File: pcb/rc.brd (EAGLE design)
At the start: 40.6 x 58.4 mm, 57 parts, among them IC2 TP4056

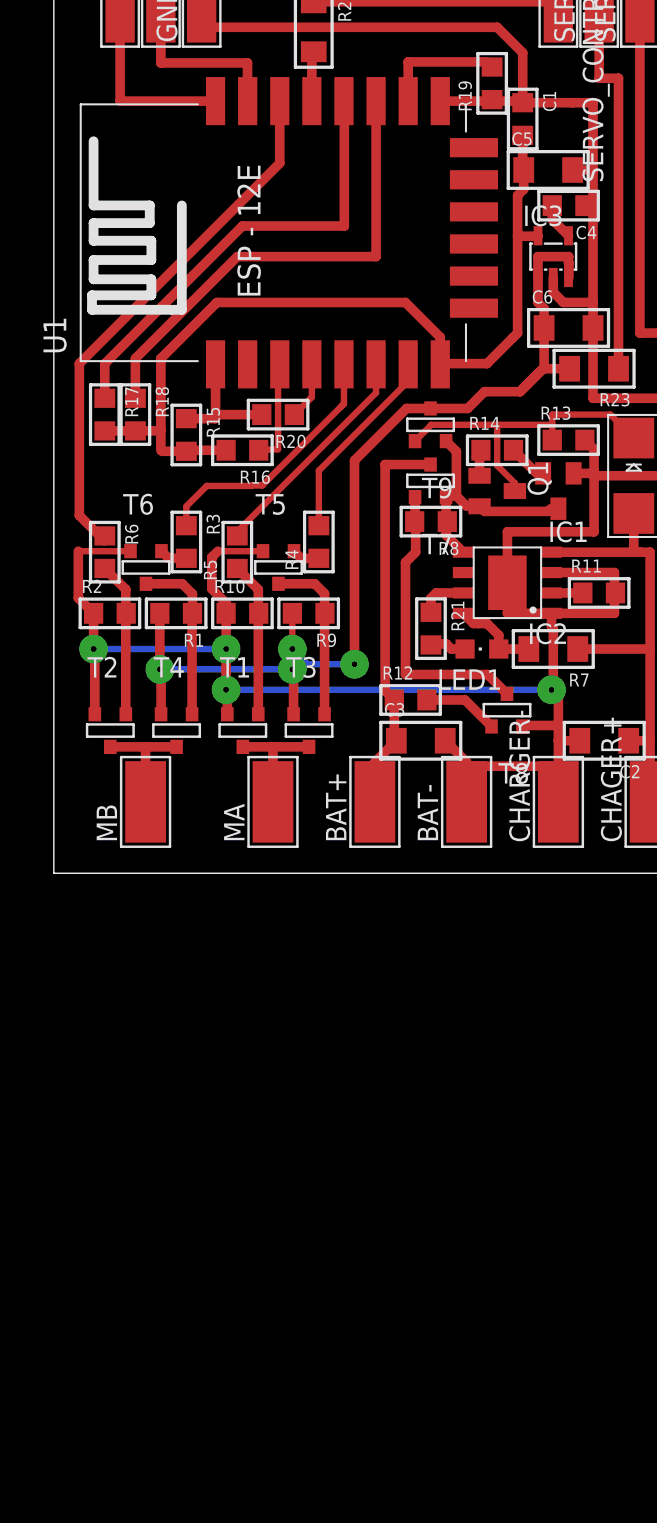
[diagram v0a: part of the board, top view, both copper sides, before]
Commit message: scheme: change H-bridge and battety check
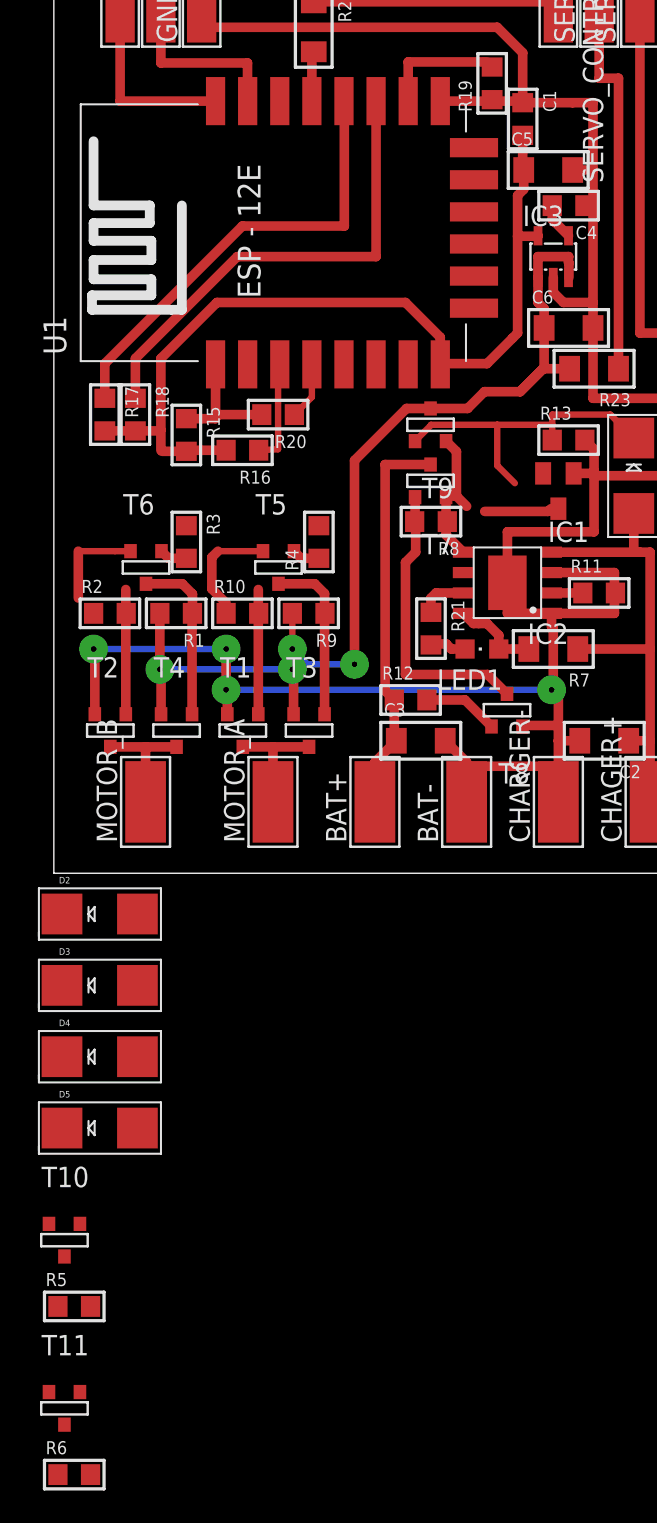
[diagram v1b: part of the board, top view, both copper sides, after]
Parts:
- removed Q1: (no value), semicon-smd-ipc:SOT23
- removed R14: (no value), skydrop:R0805
- added D2, D3, D4, D5: (no value), skydrop:SMADIODE
- added T10, T11: (no value), zetex:SOT-23
- moved R6 57.5 mm to (1.27, -33.0), turned to 0 degrees
- moved R5 48.1 mm to (1.27, -22.5), turned to 0 degrees
- renumbered MA to MOTOR_A, MB to MOTOR_B
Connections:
- removed net H_LN: R5.2, U1.GPIO12
- removed net H_LP: R4.2, U1.GPIO13
- removed net H_RN: R6.1, U1.GPIO5
- removed net H_RP: R3.1, U1.GPIO14
- new net BAT_CHECK: T11.1, U1.GPIO12
- new net H_BCK: R3.1, U1.GPIO13
- new net H_FWD: R4.2, U1.GPIO14
- new net H_PWM: R5.2, U1.GPIO5
- new net N$31: D4.C, D5.C, T10.1
- new net N$32: R5.1, T10.3
- net BAT_PROT: now also R10.1, R2.1
- net GND: now also T10.2, T11.2; no longer R10.1, R2.1
- net N$1: now also D2.C
- net N$10: no longer Q1.2
- net N$13: now also R6.2, T11.3; no longer Q1.1, R14.1
- net N$17: now also R6.1; no longer R14.2
- net N$24: no longer Q1.3
- net N$6: now also D2.A, D4.A; no longer R5.1
- net N$8: now also D3.C
- net N$9: now also D3.A, D5.A; no longer R6.2
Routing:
- net H_RN: track 33.6 -> 0.00 mm
- net H_RP: track 16.4 -> 0.00 mm
- net H_LN: track 14.3 -> 0.00 mm
- net H_LP: track 12.4 -> 0.00 mm
- net GND: track 219.5 -> 213.1 mm
- net N$17: track 2.44 -> 0.00 mm
- net N$9: track 9.65 -> 7.80 mm
- net N$6: track 9.70 -> 7.85 mm
- net N$13: track 1.71 -> 0.00 mm
- net N$10: track 15.4 -> 14.1 mm

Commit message: begin pcb v2
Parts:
- removed CHAGER+, CHARGER-: WIREPADSMD5-2,5, wirepad:5-2,5
- removed D1, D5: (no value), skydrop:SMADIODE
- added D6: (no value), skydrop:SOD-123FL
- added J1: (no value), skydrop:USB-AB-MICRO-SMD
- added R14: 0, skydrop:R1206
- added R24: (no value), skydrop:R1206
- D2, D3, D4: device skydrop:SMADIODE -> skydrop:SOD-123FL
- moved GND 54.7 mm to (5.40, 4.13), flipped to the bottom, turned to 180 degrees
- moved RX 54.7 mm to (2.86, 4.13), flipped to the bottom, turned to 0 degrees
- moved TX 54.7 mm to (0.32, 4.13), flipped to the bottom, turned to 0 degrees
- moved SERVO_CONTROL 51.8 mm to (28.9, 6.99), flipped to the bottom, turned to 0 degrees
- moved SERVO_GND 51.8 mm to (34.0, 6.99), flipped to the bottom, turned to 180 degrees
- moved SERVO_POWER 51.8 mm to (31.4, 6.99), flipped to the bottom, turned to 180 degrees
- moved R22 48.6 mm to (15.2, 8.57), flipped to the bottom, turned to 90 degrees
- moved R5 46.4 mm to (7.30, 23.5), turned to 90 degrees
- moved R6 41.9 mm to (18.7, 5.08), turned to 90 degrees
- moved T10 41.7 mm to (3.81, 23.2), turned to 90 degrees
- moved R19 41.7 mm to (24.8, 12.1), flipped to the bottom, turned to 270 degrees
- moved T11 39.2 mm to (21.3, 4.45), turned to 90 degrees
- moved C1 37.2 mm to (26.7, 14.3), flipped to the bottom, turned to 90 degrees
- moved C5 30.9 mm to (28.3, 17.5), flipped to the bottom, turned to 180 degrees
- moved IC1 29.0 mm to (15.9, 3.81), turned to 90 degrees
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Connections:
- net N$14 renamed BAT+
- net N$15 renamed TX
- net N$18 renamed RX
- removed net N$10: IC1.3, IC2.5, R8.1, T7.2, T9.2
- removed net N$24: D1.C, R13.1, T9.3
- new net BAT_CHRG: IC2.5, R8.1, T7.2, T9.2
- new net N$14: R14.1, T11.1
- net BAT_CHECK: now also R14.2; no longer T11.1
- net BAT_PROT: now also IC1.3
- net GND: now also J1.GND; no longer CHARGER-.1
- net N$31: now also D6.C; no longer D5.C
- net N$9: now also D6.A; no longer D5.A
- net V_CHRG: now also J1.VBUS, R13.1, R24.1, R24.2, T9.3; no longer CHAGER+.1, D1.A
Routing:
- net H_BCK: track 0.00 -> 51.2 mm, vias 0 -> 1
- net H_PWM: track 0.00 -> 49.7 mm, vias 0 -> 1
- net BAT_CHECK: track 0.00 -> 29.0 mm, vias 0 -> 1
- net N$24: track 20.4 -> 0.00 mm
- net N$12: track 19.1 -> 4.25 mm
- net GND: track 213.1 -> 198.3 mm, vias 4 -> 5
- net N$10: track 14.1 -> 0.00 mm
- net N$29: track 15.3 -> 1.59 mm
- net H_FWD: track 0.00 -> 13.3 mm, vias 0 -> 1
- net N$31: track 0.00 -> 10.4 mm
- net BAT_PROT: track 66.2 -> 56.8 mm, vias 4 -> 3
- net BAT_CHRG: track 0.00 -> 8.83 mm
- net RX: track 11.6 -> 19.9 mm
- net V_CHRG: track 30.5 -> 23.4 mm
- net TX: track 12.1 -> 17.9 mm
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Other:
- board size 40.6 x 58.4 mm -> 65.4 x 64.1 mm

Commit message: pcb
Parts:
- added GND19, GND20: WIREPADSMD5-1,8, wirepad:5-1,8
- R24: value (none) -> 0
- moved R24 49.0 mm to (29.5, 30.5), turned to 90 degrees
- moved J1 40.6 mm to (25.4, 37.1), turned to 270 degrees
- moved C2 17.8 mm to (25.4, 31.8)
- moved R7 17.3 mm to (15.6, 8.57)
- moved BAT- 9.26 mm to (54.0, 3.81)
- moved C3 9.26 mm to (51.1, 7.62)
- moved R14 9.26 mm to (30.2, 7.94)
- moved T9 9.26 mm to (33.0, 7.94)
- moved IC1 9.26 mm to (25.1, 2.86)
- moved R6 9.26 mm to (27.9, 4.13)
- moved T11 9.26 mm to (30.5, 3.49)
- moved BAT+ 9.26 mm to (48.3, 3.81)
- moved R19 9.26 mm to (34.0, 11.1)
- moved R10 8.82 mm to (6.03, 17.1)
- moved T6 8.55 mm to (13.7, 23.5)
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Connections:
- new net N$10: C2.1, J1.VBUS, R24.2
- net GND: now also GND20.1
- net N$21: now also GND19.1
- net V_CHRG: no longer C2.1, J1.VBUS, R24.2
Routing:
- net BAT_CHRG: track 8.83 -> 43.8 mm
- net VCC: track 53.3 -> 82.1 mm
- net N$4: track 11.0 -> 27.2 mm
- net V_CHRG: track 23.4 -> 7.64 mm
- net H_PWM: track 49.7 -> 34.6 mm
- net RX: track 19.9 -> 6.94 mm
- net N$26: track 7.72 -> 19.0 mm
- net N$33: track 11.0 -> 4.80 mm
- net N$9: track 8.65 -> 14.8 mm
- net N$10: track 0.00 -> 5.67 mm
- net H_BCK: track 51.2 -> 45.8 mm
- net N$31: track 10.4 -> 5.14 mm
- net N$32: track 5.77 -> 2.82 mm
- net BAT_PROT: track 56.8 -> 59.5 mm, vias 3 -> 1
- net BAT_CHECK: track 29.0 -> 31.5 mm
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
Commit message: pcb
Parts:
- removed GND19, GND20: WIREPADSMD5-1,8, wirepad:5-1,8
- added FLASH1, FLASH2: WIREPADSMD5-1,8, wirepad:5-1,8
- added JP1, JP2, JP5: (no value), adafruit:1X03
- added JP3, JP4: (no value), adafruit:1X01
- moved R7 18.9 mm to (30.2, 20.6)
- moved R22 4.51 mm to (18.1, 9.21), turned to 0 degrees
- moved BAT+ 3.27 mm to (49.8, 6.67)
- moved BAT- 3.27 mm to (55.6, 6.67)
- moved C3 3.27 mm to (52.7, 10.5)
- moved R14 3.18 mm to (30.2, 11.1)
- moved T9 3.18 mm to (33.0, 11.1)
- moved T11 3.18 mm to (30.5, 6.67)
- moved IC1 3.17 mm to (25.1, 6.03)
- moved R12 3.17 mm to (38.1, 8.57)
- moved R13 3.17 mm to (33.3, 7.30)
- moved R6 3.17 mm to (27.9, 7.30)
- moved R8 3.17 mm to (41.0, 11.4)
- moved T7 3.17 mm to (38.1, 11.4)
- moved T8 3.17 mm to (44.1, 9.84)
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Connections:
- net GND: now also FLASH2.1; no longer GND20.1
- net N$21: now also FLASH1.1; no longer GND19.1
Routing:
- net BAT_PROT: track 59.5 -> 171.4 mm
- net GND: track 200.4 -> 286.0 mm, vias 2 -> 1
- net VCC: track 82.1 -> 53.7 mm
- net V_CHRG: track 7.64 -> 34.2 mm, vias 0 -> 2
- net H_BCK: track 45.8 -> 19.7 mm
- net N$29: track 1.59 -> 19.4 mm
- net N$21: track 27.9 -> 40.2 mm
- net N$33: track 4.80 -> 16.8 mm
- net RX: track 6.94 -> 16.7 mm
- net BAT_CHECK: track 31.5 -> 38.4 mm
- net SERVO_CONTROL: track 1.74 -> 8.59 mm
- net H_FWD: track 12.9 -> 18.2 mm
- net H_PWM: track 34.6 -> 39.3 mm
- net N$4: track 27.2 -> 23.1 mm
- net N$26: track 19.0 -> 15.3 mm
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
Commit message: pcb
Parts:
- added C7: (no value), skydrop:C0805
- added C8, C9: (no value), adafruit:D/7343-31W
- added D5: (no value), adafruit:SMADIODE
- added IC4: (no value), my:SOT23-5
- added L1: (no value), inductor-neosid:MS85
- added R25: 0, skydrop:R1206
- added T12: (no value), zetex:SOT-23
- IC2: device TP4056:SOP-8 -> my:SOP-8
- moved R24 3.59 mm to (32.1, 33.0)
- moved IC2 3.18 mm to (25.1, 27.9)
- moved R11 3.18 mm to (30.8, 27.3)
- moved R21 3.18 mm to (20.3, 25.1)
- moved R7 3.18 mm to (30.2, 23.8)
- moved LED1 2.86 mm to (23.5, 23.5)
- moved R3 1.27 mm to (13.3, 27.6)
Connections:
- new net N$15: IC4.5, T12.3
- new net N$18: IC4.1, R25.1
- new net N$24: C9.+, L1.1, R25.2
- new net N$3: D5.A, L1.2, T12.1
- new net N$34: C7.2, C8.+, D5.C, IC4.2
- net GND: now also C7.1, C8.-, C9.-, IC2.HEATSINK, IC4.4, T12.2
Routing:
- net GND: track 286.0 -> 340.1 mm
- net N$34: track 0.00 -> 24.1 mm
- net N$24: track 0.00 -> 10.0 mm
- net N$3: track 0.00 -> 9.28 mm
- net V_CHRG: track 34.2 -> 41.3 mm
- net BAT_CHRG: track 40.6 -> 43.8 mm
- net N$18: track 0.00 -> 2.93 mm
- net N$10: track 5.67 -> 8.56 mm
- net BAT_CHECK: track 38.4 -> 40.3 mm
- net N$15: track 0.00 -> 1.53 mm
- net H_FWD: track 18.2 -> 16.9 mm
- net N$7: track 2.13 -> 2.67 mm

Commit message: pcb
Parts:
- added R26, R27, R28: 0, skydrop:R1206
- moved R19 29.3 mm to (3.49, 21.9), turned to 90 degrees
- moved R15 19.1 mm to (26.7, 34.6), turned to 180 degrees
- moved C5 18.2 mm to (45.4, 23.5)
- moved C4 18.2 mm to (46.7, 25.7)
- moved C6 18.2 mm to (46.7, 33.3)
- moved IC3 18.2 mm to (45.7, 28.9)
- moved R23 18.2 mm to (48.3, 35.9)
- moved C1 18.2 mm to (43.8, 20.3)
- moved R16 17.9 mm to (27.6, 31.4), turned to 90 degrees
- moved R20 14.7 mm to (25.7, 30.2), turned to 90 degrees
- moved T10 8.31 mm to (7.94, 32.4)
- moved D6 7.96 mm to (6.03, 29.5)
- moved R5 7.69 mm to (10.5, 33.7)
- moved D4 6.68 mm to (7.94, 28.3)
- moved R4 6.43 mm to (13.0, 33.7)
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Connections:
- new net N$35: R26.2, R27.1
- new net N$36: MOTOR_A.1, R27.2
- new net N$37: R28.2, T4.1
- net BAT_CHECK: now also U1.GPIO14; no longer U1.GPIO12
- net H_BCK: now also U1.GPIO12; no longer U1.GPIO13
- net H_FWD: now also U1.GPIO13; no longer U1.GPIO14
- net N$33: now also R26.1; no longer MOTOR_A.1
- net N$4: now also R28.1; no longer T4.1
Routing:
- net GND: track 340.1 -> 308.8 mm
- net BAT_PROT: track 171.4 -> 144.6 mm
- net VCC: track 53.7 -> 76.6 mm, vias 0 -> 2
- net H_PWM: track 39.3 -> 18.9 mm
- net H_BCK: track 20.0 -> 39.6 mm
- net H_FWD: track 16.9 -> 34.3 mm
- net TX: track 16.9 -> 33.1 mm
- net RX: track 16.7 -> 31.8 mm
- net BAT_CHECK: track 40.3 -> 27.0 mm
- net N$33: track 16.8 -> 3.81 mm
- net N$26: track 15.3 -> 3.23 mm
- net SERVO_CONTROL: track 8.59 -> 20.6 mm
- net N$36: track 0.00 -> 10.5 mm
- net V_CHRG: track 41.3 -> 33.9 mm
- net N$37: track 0.00 -> 6.69 mm
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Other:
- board size 65.4 x 64.1 mm -> 64.8 x 69.2 mm

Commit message: pcb
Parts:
- added R29: 0, skydrop:R1206
- U1: device esp8266modules:ESP12E-SMD -> my:ESP-12
- moved C9 36.5 mm to (32.7, 19.4), flipped to the bottom, turned to 180 degrees
- moved C5 35.3 mm to (11.4, 14.0), turned to 270 degrees
- moved C4 35.3 mm to (13.7, 13.3), turned to 90 degrees
- moved C6 33.1 mm to (20.3, 13.3), turned to 270 degrees
- moved IC3 32.4 mm to (16.8, 14.3), turned to 270 degrees
- moved R25 31.5 mm to (32.7, 23.8), flipped to the bottom, turned to 180 degrees
- moved R21 30.8 mm to (54.0, 32.7)
- moved C7 30.5 mm to (29.8, 21.9), flipped to the bottom, turned to 0 degrees
- moved L1 28.9 mm to (35.9, 29.5), flipped to the bottom, turned to 0 degrees
- moved LED1 27.8 mm to (54.6, 26.7)
- moved C1 25.9 mm to (18.1, 17.5), turned to 180 degrees
- moved IC4 25.4 mm to (30.5, 27.9), flipped to the bottom, turned to 0 degrees
- moved T12 22.7 mm to (30.5, 31.8), flipped to the bottom, turned to 180 degrees
- moved D5 21.6 mm to (32.7, 36.2), flipped to the bottom, turned to 180 degrees
- moved C8 20.7 mm to (32.7, 40.0), flipped to the bottom, turned to 0 degrees
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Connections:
- removed net N$34: C7.2, C8.+, D5.C, IC4.2
- new net 5V: C7.2, C8.+, D5.C, IC4.2, R23.2, R29.2
- net BAT_CHECK: now also U1.GPIO13; no longer U1.GPIO14
- net BAT_PROT: now also C9.+, L1.1, R25.2; no longer C6.1, IC3.1, IC3.3, R23.2
- net H_BCK: now also U1.GPIO14; no longer U1.GPIO12
- net H_FWD: now also U1.GPIO12; no longer U1.GPIO13
- net N$24: now also C6.1, IC3.1, IC3.3, R29.1; no longer C9.+, L1.1, R25.2
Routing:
- net BAT_PROT: track 144.6 -> 76.5 mm
- net GND: track 308.8 -> 242.2 mm
- net 5V: track 0.00 -> 52.9 mm
- net N$34: track 24.1 -> 0.00 mm
- net N$30: track 23.5 -> 0.00 mm
- net V_CHRG: track 33.9 -> 53.8 mm
- net N$22: track 23.9 -> 4.29 mm, vias 0 -> 1
- net N$21: track 37.3 -> 19.3 mm, vias 0 -> 1
- net H_PWM: track 18.9 -> 4.58 mm
- net BAT_CHECK: track 27.0 -> 13.0 mm
- net N$23: track 3.40 -> 17.3 mm
- net BAT_CHRG: track 40.6 -> 27.3 mm
- net H_FWD: track 34.3 -> 44.8 mm
- net H_BCK: track 39.6 -> 47.4 mm
- net BAT+: track 23.8 -> 17.8 mm
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
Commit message: pcb
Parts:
- removed JP4: (no value), adafruit:1X01
- removed JP5: (no value), adafruit:1X03
- added JP6: (no value), pinhead:1X02
- JP1, JP2: device adafruit:1X03 -> pinhead:1X03
- JP3: device adafruit:1X01 -> pinhead:1X03
- moved JP1 55.4 mm to (6.03, 4.13)
- moved JP3 51.1 mm to (2.22, 4.13), turned to 90 degrees
- moved JP2 43.5 mm to (13.3, 4.13)
- moved R23 10.0 mm to (43.2, 9.53)
- moved R29 5.72 mm to (18.4, 14.6)
- moved C4 5.71 mm to (7.94, 13.3)
- moved C5 5.71 mm to (5.71, 14.0)
- moved C6 5.71 mm to (14.6, 13.3)
- moved IC3 5.71 mm to (11.1, 14.3)
- moved T9 4.85 mm to (25.7, 17.8)
- moved C1 4.45 mm to (13.7, 17.5)
- moved R13 3.31 mm to (26.7, 10.8)
- moved T8 2.88 mm to (34.9, 17.1)
- moved R8 2.86 mm to (32.1, 18.7)
- moved T7 2.86 mm to (29.2, 18.7)
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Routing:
- net GND: track 242.2 -> 277.1 mm, vias 1 -> 2
- net BAT_PROT: track 76.5 -> 62.3 mm
- net V_CHRG: track 53.8 -> 43.7 mm
- net N$36: track 11.2 -> 3.87 mm
- net BAT_CHRG: track 27.3 -> 21.2 mm
- net VCC: track 73.1 -> 76.1 mm
- net 5V: track 52.9 -> 55.0 mm
- net BAT_CHECK: track 13.0 -> 14.7 mm
- net N$4: track 22.0 -> 23.4 mm
- net N$29: track 14.7 -> 13.4 mm
- net BAT+: track 17.8 -> 18.9 mm
